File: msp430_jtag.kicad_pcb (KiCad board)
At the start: 2 copper layers, 57.2 x 38.1 mm, 25 parts, among them P1 CONN_01X25, P2 CONN_01X07, P3 CONN_01X02, Q1 PN2222A, U1 74LS244

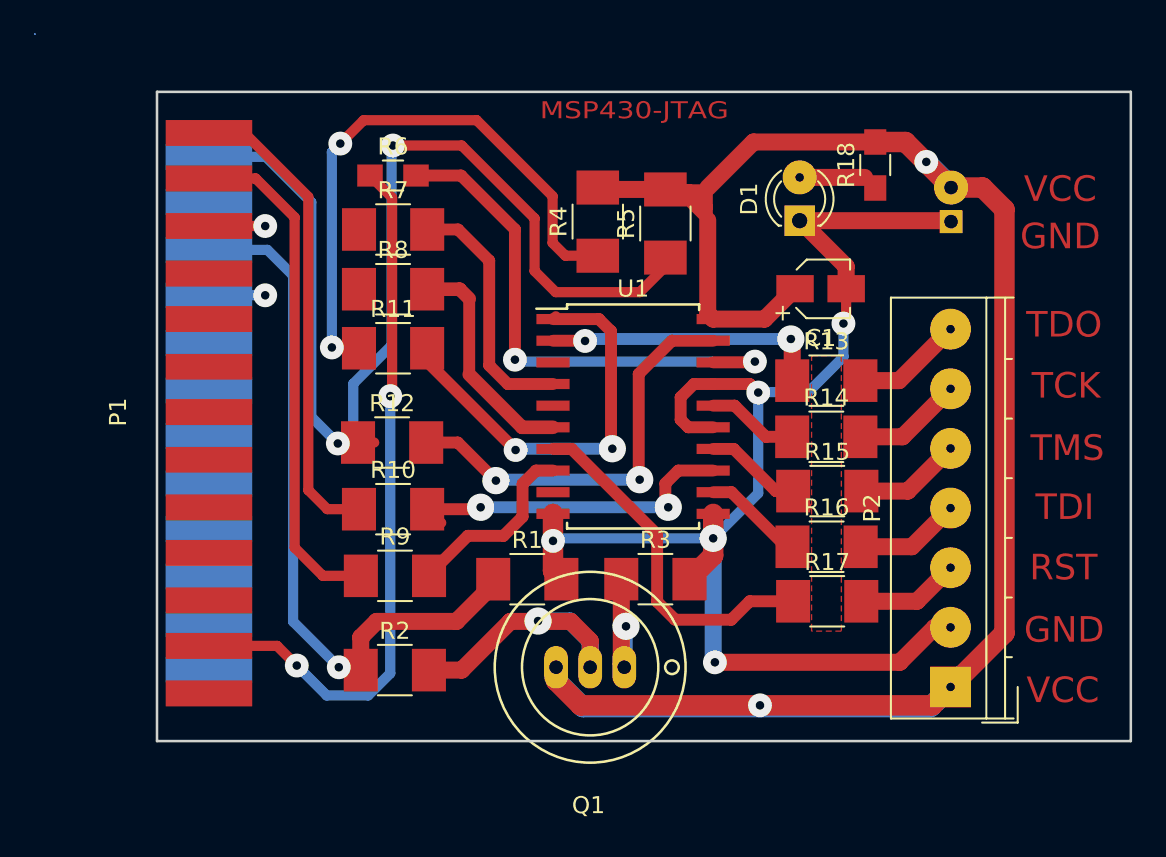
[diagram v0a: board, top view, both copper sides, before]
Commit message: *fixed 2 net-connection
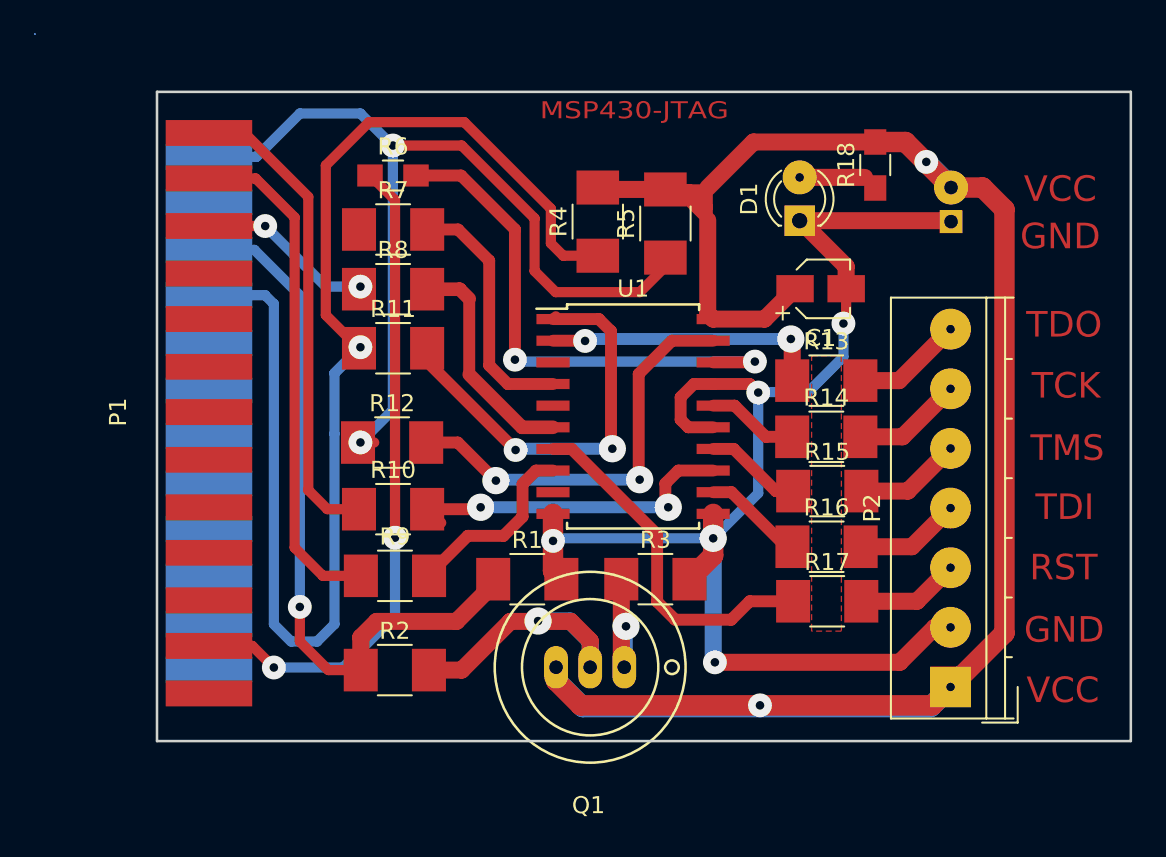
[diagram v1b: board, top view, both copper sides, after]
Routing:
- net Net-(P1-Pad17): track 38.6 -> 81.4 mm, vias 3 -> 1
- net Net-(P1-Pad14): track 68.7 -> 57.7 mm
- net Net-(P1-Pad3): track 3.30 -> 10.8 mm, vias 1 -> 2
- net Net-(P1-Pad12): track 47.4 -> 44.4 mm
- net Net-(P1-Pad16): track 46.6 -> 47.5 mm

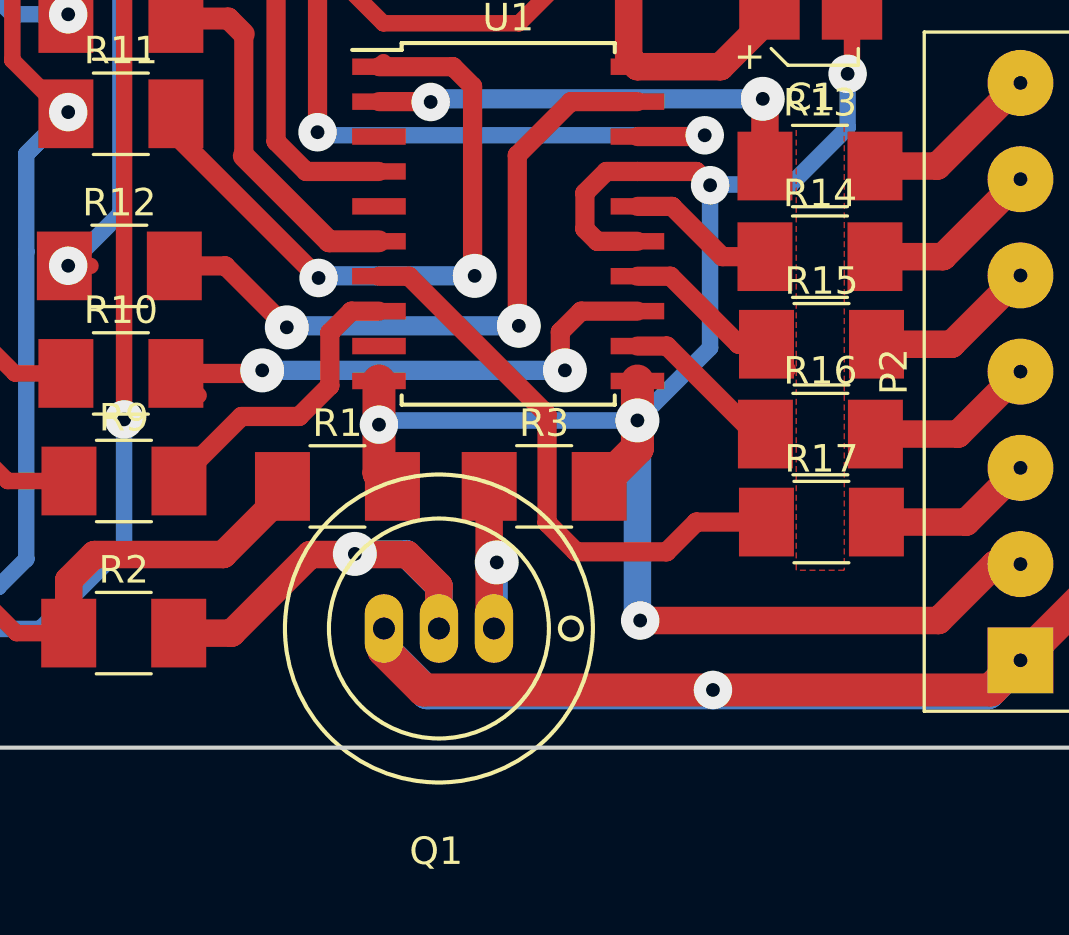
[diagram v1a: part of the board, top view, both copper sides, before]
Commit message: *change transistor footprint
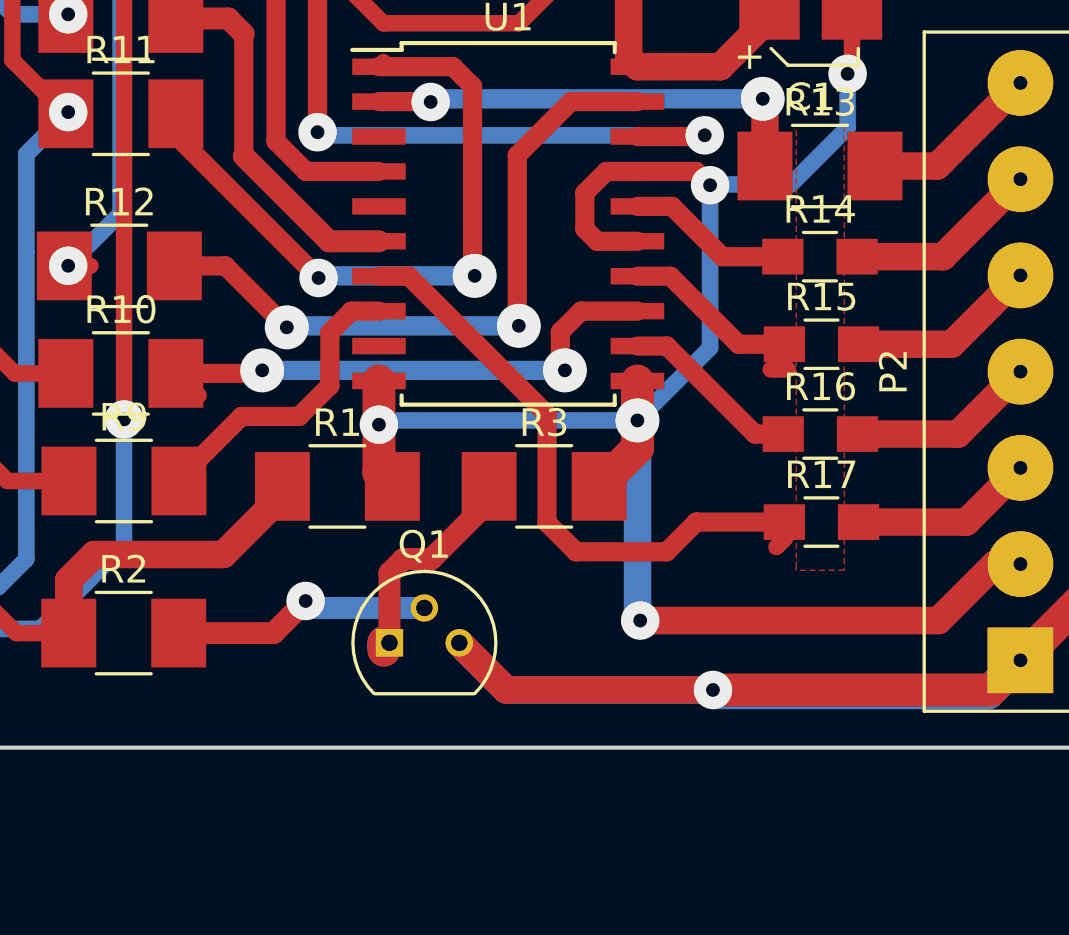
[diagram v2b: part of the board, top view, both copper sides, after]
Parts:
- Q1: footprint Transistors_OldSowjetAera:OldSowjetaera_Transistor_Type-I_BigPads -> TO_SOT_Packages_THT:TO-92_Molded_Narrow
- R14, R15, R16, R17: footprint Resistors_SMD:R_1210_HandSoldering -> Resistors_SMD:R_0805_HandSoldering
- moved Q1 1.87 mm to (144.3, 119.4), turned to 0 degrees
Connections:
- P1 pad 10: Net-(P1-Pad10) -> (no net)
- P1 pad 11: Net-(P1-Pad11) -> (no net)
- P1 pad 13: Net-(P1-Pad13) -> (no net)
- P1 pad 15: Net-(P1-Pad15) -> (no net)
- P1 pad 5: Net-(P1-Pad5) -> (no net)
- P1 pad 6: Net-(P1-Pad6) -> (no net)
- P1 pad 7: Net-(P1-Pad7) -> (no net)
- P1 pad 8: Net-(P1-Pad8) -> (no net)
- P1 pad 9: Net-(P1-Pad9) -> (no net)
- U1 pad 3: Net-(U1-Pad3) -> (no net)
- U1 pad 5: Net-(U1-Pad5) -> (no net)
- U1 pad 9: Net-(U1-Pad9) -> (no net)
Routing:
- net (no net): track 0.00 -> 15.2 mm
- net Net-(P1-Pad10): track 8.57 -> 0.00 mm
- net Net-(Q1-Pad2): track 17.8 -> 9.52 mm
- net VCC: track 130.0 -> 122.9 mm
- net Net-(P1-Pad11): track 6.02 -> 0.00 mm
- net Net-(Q1-Pad1): track 7.98 -> 9.48 mm, vias 1 -> 0
- net Net-(R15-Pad1): track 6.34 -> 5.72 mm
